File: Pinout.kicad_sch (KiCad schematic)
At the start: 4 parts, among them J7 Conn_01x02_Pin, J8 Conn_01x02_Pin

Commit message: "Update KiRA Flight Computer schematic and PCB files"
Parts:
- added BZ1: Buzzer, symbol Device:Buzzer
- added J10: Conn_01x02_Pin, Connector_PinHeader_2.54mm:PinHeader_1x02_P2.54mm_Vertical, symbol Connector:Conn_01x02_Pin
- J7, J8: footprint (none) -> Connector_PinHeader_2.54mm:PinHeader_1x02_P2.54mm_Vertical
- R18, R19: footprint (none) -> Resistor_SMD:R_0603_1608Metric
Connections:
- new net BUZZER: BZ1.1 (+)
- new net GND: BZ1.2 (-)
- new net UART2_RX: J10.2 (Pin_2)
- new net UART2_TX: J10.1 (Pin_1)
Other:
- moved on the sheet: J7

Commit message: Update PCB
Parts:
- removed J7: Conn_01x02_Pin, Connector_PinHeader_2.54mm:PinHeader_1x02_P2.54mm_Vertical, symbol Connector:Conn_01x02_Pin
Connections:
- net UART2_RX: now also J10.1 (Pin_1); no longer J10.2 (Pin_2)
- net UART2_TX: now also J10.2 (Pin_2); no longer J10.1 (Pin_1)
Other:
- moved on the sheet: J10
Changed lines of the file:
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@@
 		)
 	)
-	(global_label "UART1_RX"
+	(global_label "I2C3_SCL"
 		(shape input)
-		(at 48.26 36.83 180)
+		(at 39.37 69.85 180)
 		(fields_autoplaced yes)
 		(effects
@@
 		)
 		(property "Intersheetrefs" "${INTERSHEET_REFS}"
-			(at 35.9615 36.83 0)
-			(effects
-				(font
-					(size 1.27 1.27)
-				)
-				(justify right)
-				(hide yes)
-			)
-		)
-	)
-	(global_label "UART1_TX"
+			(at 27.6158 69.85 0)
+			(effects
+				(font
+					(size 1.27 1.27)
+				)
+				(justify right)
+				(hide yes)
+			)
+		)
+	)
+	(global_label "I2C3_SDA"
 		(shape input)
-		(at 48.26 39.37 180)
+		(at 39.37 67.31 180)
 		(fields_autoplaced yes)
 		(effects
@@
 		)
 		(property "Intersheetrefs" "${INTERSHEET_REFS}"
-			(at 36.2639 39.37 0)
-			(effects
-				(font
-					(size 1.27 1.27)
-				)
-				(justify right)
-				(hide yes)
-			)
-		)
-	)
-	(global_label "I2C3_SCL"
+			(at 27.5553 67.31 0)
+			(effects
+				(font
+					(size 1.27 1.27)
+				)
+				(justify right)
+				(hide yes)
+			)
+		)
+	)
+	(global_label "UART2_RX"
 		(shape input)
-		(at 39.37 69.85 180)
+		(at 48.26 41.91 180)
 		(fields_autoplaced yes)
 		(effects
@@
 		)
 		(property "Intersheetrefs" "${INTERSHEET_REFS}"
-			(at 27.6158 69.85 0)
-			(effects
-				(font
-					(size 1.27 1.27)
-				)
-				(justify right)
-				(hide yes)
-			)
-		)
-	)
-	(global_label "I2C3_SDA"
+			(at 35.9615 41.91 0)
+			(effects
+				(font
+					(size 1.27 1.27)
+				)
+				(justify right)
+				(hide yes)
+			)
+		)
+	)
+	(global_label "UART2_TX"
 		(shape input)
-		(at 39.37 67.31 180)
+		(at 48.26 44.45 180)
 		(fields_autoplaced yes)
 		(effects
@@
 		)
 		(property "Intersheetrefs" "${INTERSHEET_REFS}"
-			(at 27.5553 67.31 0)
-			(effects
-				(font
-					(size 1.27 1.27)
-				)
-				(justify right)
-				(hide yes)
-			)
-		)
-	)
-	(global_label "UART2_RX"
-		(shape input)
-		(at 48.26 41.91 180)
-		(fields_autoplaced yes)
-		(effects
-			(font
-				(size 1.27 1.27)
-			)
-			(justify right)
-		)
-		(property "Intersheetrefs" "${INTERSHEET_REFS}"
-			(at 35.9615 41.91 0)
-			(effects
-				(font
-					(size 1.27 1.27)
-				)
-				(justify right)
-				(hide yes)
-			)
-		)
-	)
-	(global_label "UART2_TX"
-		(shape input)
-		(at 48.26 44.45 180)
-		(fields_autoplaced yes)
-		(effects
-			(font
-				(size 1.27 1.27)
-			)
-			(justify right)
-		)
-		(property "Intersheetrefs" "${INTERSHEET_REFS}"
 			(at 36.2639 44.45 0)
 			(effects
@@
 	(symbol
 		(lib_id "Connector:Conn_01x02_Pin")
-		(at 53.34 39.37 180)
-		(unit 1)
-		(exclude_from_sim no)
-		(in_bom yes)
-		(on_board yes)
-		(dnp no)
-		(fields_autoplaced yes)
-		(property "Reference" "J7"
-			(at 54.61 36.8299 0)
+		(at 53.34 41.91 0)
+		(mirror y)
+		(unit 1)
+		(exclude_from_sim no)
+		(in_bom yes)
+		(on_board yes)
+		(dnp no)
+		(property "Reference" "J10"
+			(at 54.61 44.4501 0)
 			(effects
 				(font
@@
 		)
 		(property "Value" "Conn_01x02_Pin"
-			(at 54.61 39.3699 0)
+			(at 54.61 41.9101 0)
 			(effects
 				(font
@@
 		)
 		(property "Footprint" "Connector_PinHeader_2.54mm:PinHeader_1x02_P2.54mm_Vertical"
-			(at 53.34 39.37 0)
+			(at 53.34 41.91 0)
 			(effects
 				(font
@@
 		)
 		(property "Datasheet" "~"
-			(at 53.34 39.37 0)
+			(at 53.34 41.91 0)
 			(effects
 				(font
@@
 		)
 		(property "Description" "Generic connector, single row, 01x02, script generated"
-			(at 53.34 39.37 0)
-			(effects
-				(font
-					(size 1.27 1.27)
-				)
-				(hide yes)
-			)
-		)
-		(pin "1"
-		)
-		(pin "2"
-		)
-		(instances
-			(project ""
-				(path "/aff8106b-a9b7-4e48-85ad-25b2eb3ce379/b67f38d8-38f4-48c0-8f3f-0b1ef1ce702f"
-					(reference "J7")
-					(unit 1)
-				)
-			)
-		)
-	)
-	(symbol
-		(lib_id "Connector:Conn_01x02_Pin")
-		(at 53.34 44.45 180)
-		(unit 1)
-		(exclude_from_sim no)
-		(in_bom yes)
-		(on_board yes)
-		(dnp no)
-		(fields_autoplaced yes)
-		(property "Reference" "J10"
-			(at 54.61 41.9099 0)
-			(effects
-				(font
-					(size 1.27 1.27)
-				)
-				(justify right)
-			)
-		)
-		(property "Value" "Conn_01x02_Pin"
-			(at 54.61 44.4499 0)
-			(effects
-				(font
-					(size 1.27 1.27)
-				)
-				(justify right)
-			)
-		)
-		(property "Footprint" "Connector_PinHeader_2.54mm:PinHeader_1x02_P2.54mm_Vertical"
-			(at 53.34 44.45 0)
-			(effects
-				(font
-					(size 1.27 1.27)
-				)
-				(hide yes)
-			)
-		)
-		(property "Datasheet" "~"
-			(at 53.34 44.45 0)
-			(effects
-				(font
-					(size 1.27 1.27)
-				)
-				(hide yes)
-			)
-		)
-		(property "Description" "Generic connector, single row, 01x02, script generated"
-			(at 53.34 44.45 0)
+			(at 53.34 41.91 0)
 			(effects
 				(font
@@
 		(on_board yes)
 		(dnp no)
-		(fields_autoplaced yes)
 		(property "Reference" "J8"
 			(at 67.31 67.3099 0)

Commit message: Update PCB
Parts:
- added J11, J12, J3, J9: Conn_01x03_Pin, Connector_PinHeader_2.54mm:PinHeader_1x03_P2.54mm_Vertical, symbol Connector:Conn_01x03_Pin
- added J13, J14: Screw_Terminal_01x02, TerminalBlock_Phoenix:TerminalBlock_Phoenix_MPT-0,5-2-2.54_1x02_P2.54mm_Horizontal, symbol Connector:Screw_Terminal_01x02
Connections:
- net GND: now also J11.3 (Pin_3), J12.3 (Pin_3), J3.3 (Pin_3), J9.3 (Pin_3)
- net UART2_RX renamed UART4_RX
- net UART2_TX renamed UART4_TX
- new net +5V: J11.2 (Pin_2), J12.2 (Pin_2), J3.2 (Pin_2), J9.2 (Pin_2)
- new net PWM1: J3.1 (Pin_1)
- new net PWM2: J9.1 (Pin_1)
- new net PWM3: J11.1 (Pin_1)
- new net PWM4: J12.1 (Pin_1)

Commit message: questionable changes
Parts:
- added Q1, Q2: FDMA430NZ, dep:FDMA430NZ, symbol FDMA430NZ:FDMA430NZ
- added R22, R24: 220R, Resistor_SMD:R_0402_1005Metric, symbol Device:R
- added R23, R25: 4.7k, Resistor_SMD:R_0603_1608Metric, symbol Device:R
- added R26, R27: 1R, Resistor_SMD:R_0603_1608Metric, symbol Device:R
- BZ1: footprint (none) -> Buzzer_Beeper:Buzzer_CUI_CPT-9019S-SMT
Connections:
- net GND: now also Q1.4 (S_1), Q1.8 (S_2), Q2.4 (S_1), Q2.8 (S_2), R23.2, R25.2
- net +BATT: now reaches J13.1 (Pin_1)
- net +BATT: now also J14.1 (Pin_1)
- net at J13.2 (Pin_2): now also R26.1
- net at J14.2 (Pin_2): now also R27.1
- new net: Q2.1 (D_1), Q2.2 (D_2), Q2.5 (D_3), Q2.6 (D_4), Q2.7 (D_5), R27.2
- new net: Q2.3 (G), R22.2, R25.1
- new net: Q1.3 (G), R23.1, R24.2
- new net: Q1.1 (D_1), Q1.2 (D_2), Q1.5 (D_3), Q1.6 (D_4), Q1.7 (D_5), R26.2
- new net PY1: R24.1
- new net PY2: R22.1
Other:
- moved on the sheet: J12, J13

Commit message: PCB Update
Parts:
- added H1, H2, H3, H4: MountingHole, MountingHole:MountingHole_2.2mm_M2_DIN965_Pad, symbol Mechanical:MountingHole
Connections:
- net PYOUT2: now reaches Q2.1 (D_1), Q2.2 (D_2), Q2.5 (D_3), Q2.6 (D_4), Q2.7 (D_5), R27.2
- net PYOUT1: now reaches Q1.1 (D_1), Q1.2 (D_2), Q1.5 (D_3), Q1.6 (D_4), Q1.7 (D_5), R26.2
- net +BATT renamed +BAT

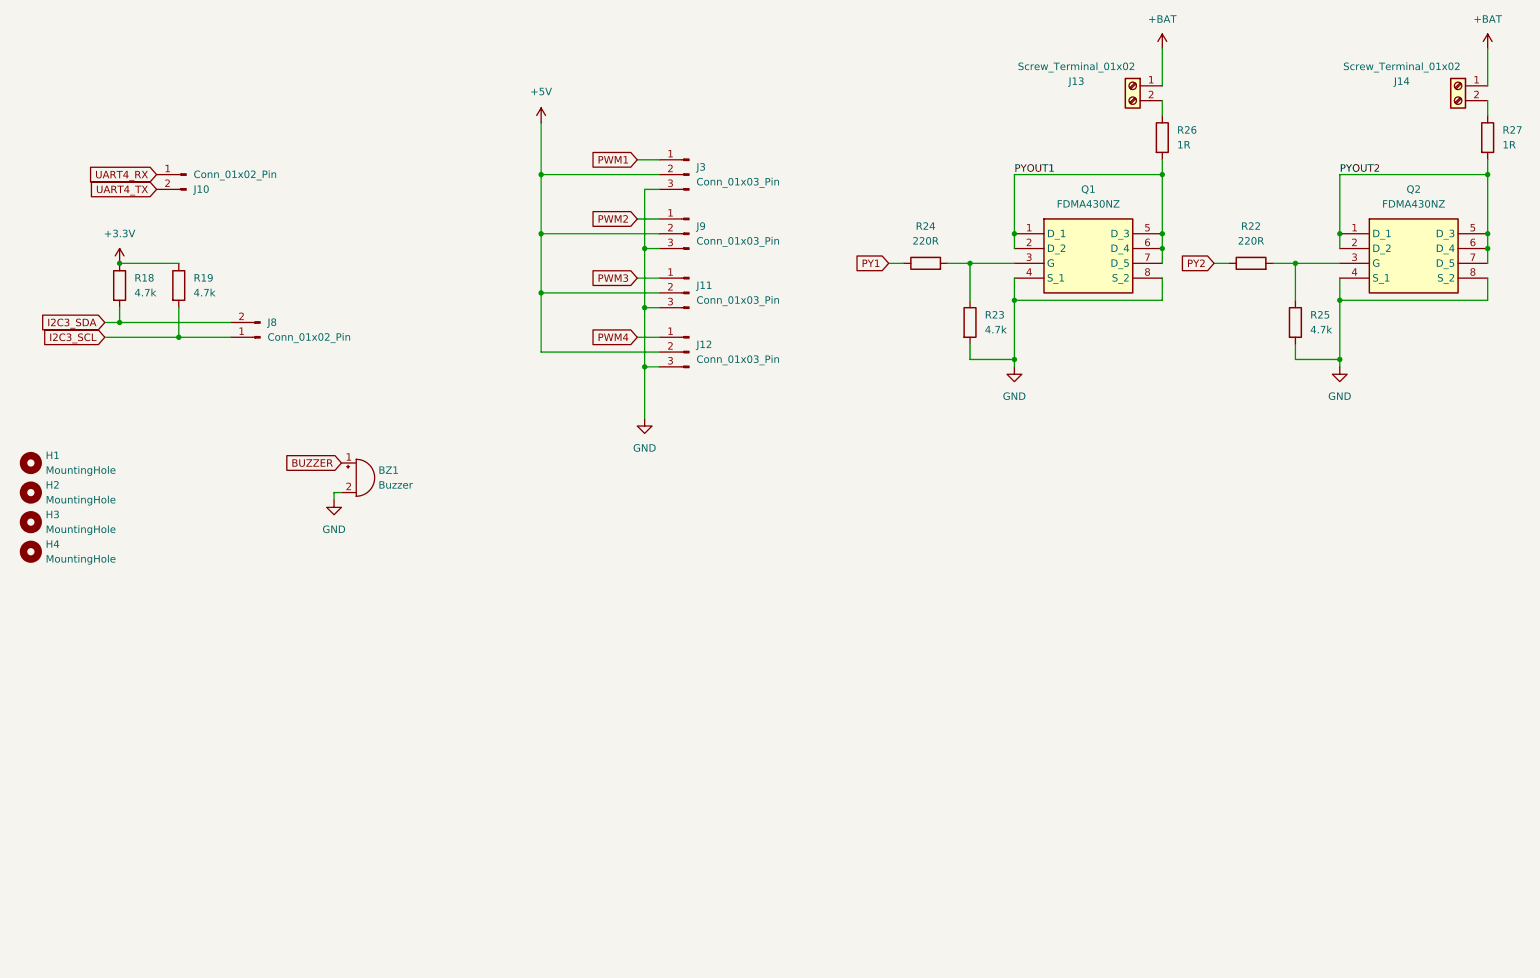
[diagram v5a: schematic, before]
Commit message: Fix
- Add decoupling cap
- Component layout
- Redraw zones
- New buck converter
- Layout tweaks
- Change connector
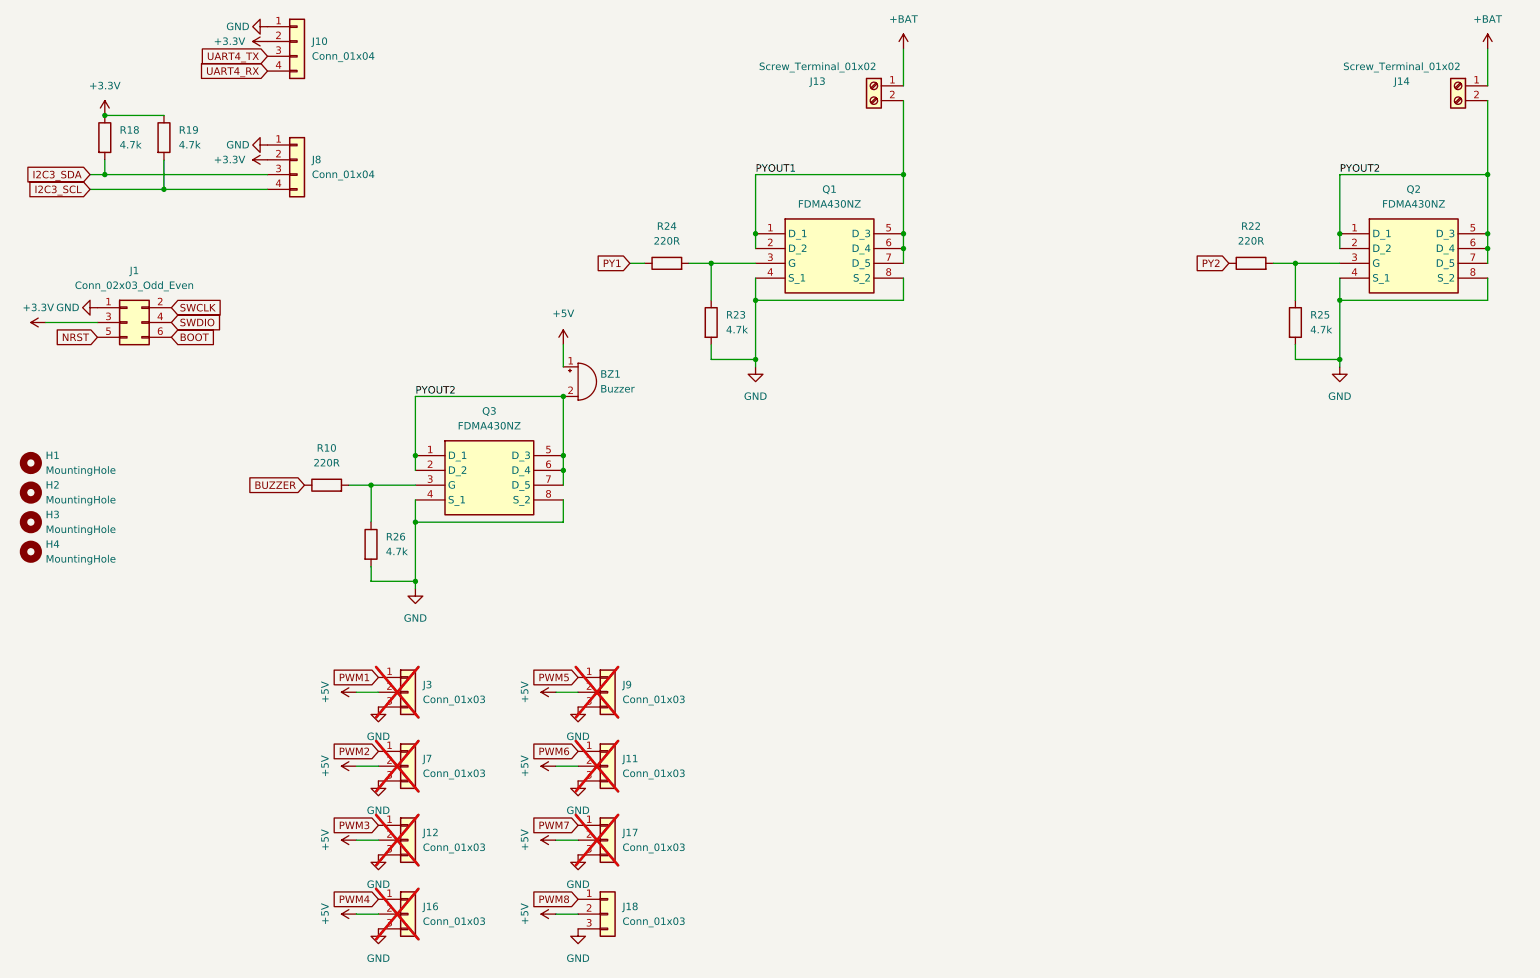
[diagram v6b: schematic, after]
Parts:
- removed J10, J8: Conn_01x02_Pin, Connector_PinHeader_2.54mm:PinHeader_1x02_P2.54mm_Vertical, symbol Connector:Conn_01x02_Pin
- removed J11, J12, J3, J9: Conn_01x03_Pin, Connector_PinHeader_2.54mm:PinHeader_1x03_P2.54mm_Vertical, symbol Connector:Conn_01x03_Pin
- removed R27: 1R, Resistor_SMD:R_0603_1608Metric, symbol Device:R
- added J1: Conn_02x03_Odd_Even, Connector_PinHeader_2.54mm:PinHeader_2x03_P2.54mm_Vertical, symbol Connector_Generic:Conn_02x03_Odd_Even
- added J10, J8: Conn_01x04, Connector_JST:JST_XH_B4B-XH-A_1x04_P2.50mm_Vertical, symbol Connector_Generic:Conn_01x04
- added J11, J12, J16, J17, J18, J3, J7, J9: Conn_01x03, Connector_PinHeader_2.54mm:PinHeader_1x03_P2.54mm_Vertical, symbol Connector_Generic:Conn_01x03
- added Q3: FDMA430NZ, dep:FDMA430NZ, symbol FDMA430NZ:FDMA430NZ
- added R10: 220R, Resistor_SMD:R_0402_1005Metric, symbol Device:R
- R26: value 1R -> 4.7k
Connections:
- net +3.3V: now also J1.3 (Pin_3), J10.2 (Pin_2), J8.2 (Pin_2)
- net +5V: now also BZ1.1 (+), J11.2 (Pin_2), J12.2 (Pin_2), J16.2 (Pin_2), J17.2 (Pin_2), J18.2 (Pin_2), J3.2 (Pin_2), J7.2 (Pin_2), J9.2 (Pin_2)
- net BUZZER: now also R10.1; no longer BZ1.1 (+)
- net GND: now also R26.2, J1.1 (Pin_1), J10.1 (Pin_1), J11.3 (Pin_3), J12.3 (Pin_3), J16.3 (Pin_3), J17.3 (Pin_3), J18.3 (Pin_3), J3.3 (Pin_3), J7.3 (Pin_3), J8.1 (Pin_1), J9.3 (Pin_3), Q3.4 (S_1), Q3.8 (S_2); no longer BZ1.2 (-)
- net I2C3_SCL: now also J8.4 (Pin_4)
- net I2C3_SDA: now also J8.3 (Pin_3)
- net PWM1: now also J3.1 (Pin_1)
- net PWM2: now also J7.1 (Pin_1)
- net PWM3: now also J12.1 (Pin_1)
- net PWM4: now also J16.1 (Pin_1)
- net PYOUT1: now also J13.2 (Pin_2); no longer R26.2
- net PYOUT2: now also BZ1.2 (-), J14.2 (Pin_2), Q3.1 (D_1), Q3.2 (D_2), Q3.5 (D_3), Q3.6 (D_4), Q3.7 (D_5)
- net UART4_RX: now also J10.4 (Pin_4)
- net UART4_TX: now also J10.3 (Pin_3)
- net at R26.1: now also Q3.3 (G), R10.2; no longer J13.2 (Pin_2)
- new net BOOT: J1.6 (Pin_6)
- new net NRST: J1.5 (Pin_5)
- new net PWM5: J9.1 (Pin_1)
- new net PWM6: J11.1 (Pin_1)
- new net PWM7: J17.1 (Pin_1)
- new net PWM8: J18.1 (Pin_1)
- new net SWCLK: J1.2 (Pin_2)
- new net SWDIO: J1.4 (Pin_4)
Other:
- moved on the sheet: BZ1, J13, Q1, R18, R19, R23, R24
